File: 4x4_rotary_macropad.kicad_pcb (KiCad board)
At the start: 4 copper layers, 77.1 x 116.4 mm, 81 parts, among them J1 Conn_01x04_Pin, J2 Conn_01x04_Socket, SW1 SW_Push, SW10 SW_Push, SW11 SW_Push, SW12 SW_Push, SW13 SW_Push, SW14 SW_Push, SW15 SW_Push, SW16 SW_Push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

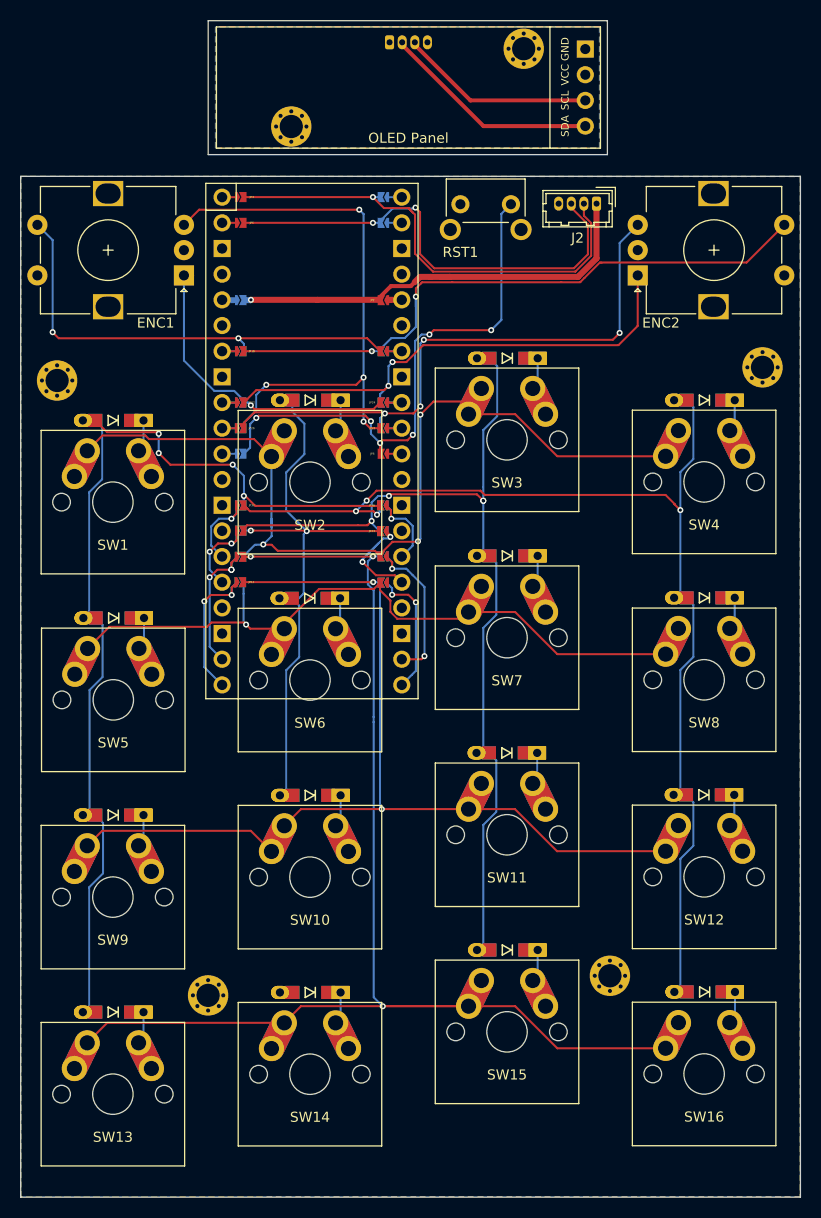
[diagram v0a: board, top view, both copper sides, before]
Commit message: Fixed JLCPCB constraints errors
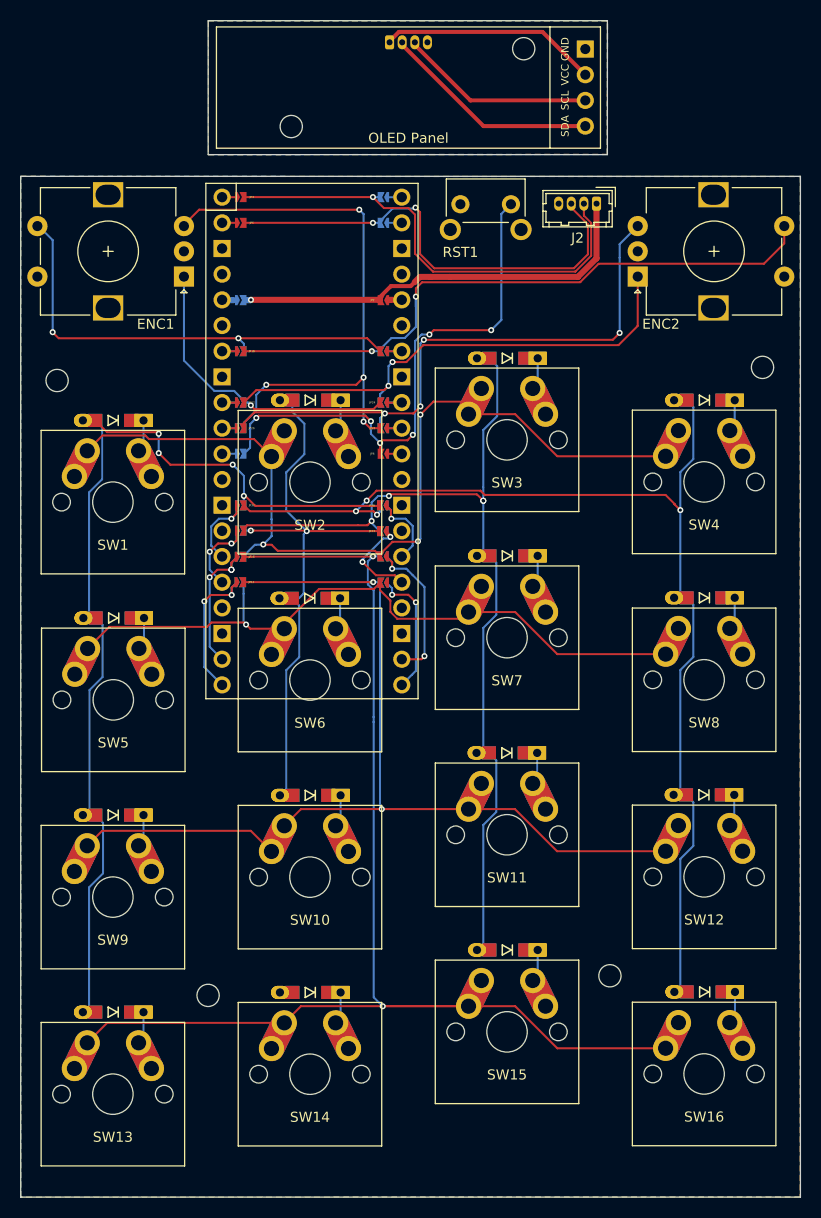
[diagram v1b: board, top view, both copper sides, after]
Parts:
- H1, H2, H3, H4, H5, H6: footprint kbd:M2_HOLE_v3 -> MountingHole:MountingHole_2.2mm_M2
- moved ENC1 0.12 mm to (44.4, 68.1)
- moved ENC2 0.12 mm to (89.2, 68.1)
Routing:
- net /B_VCC: track 0.00 -> 21.6 mm
- net C2_C1: track 11.7 -> 10.2 mm
- net R1__R2: track 16.4 -> 15.2 mm
- net ENC_1_A: track 31.3 -> 30.2 mm
- net R0: track 88.6 -> 87.5 mm
- net VCC: track 42.9 -> 42.0 mm
- net OLED_SDA: track 47.1 -> 46.5 mm
- net ENC_2_A: track 50.7 -> 50.1 mm
- net C3: track 110.6 -> 110.1 mm
- net ENC_2_SW: track 62.7 -> 63.3 mm
- net R3: vias 3 -> 2
- added copper zone on F.Cu, net /B_GND
- removed copper zone on F.Cu, net /B_VCC

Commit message: Added missing libraries
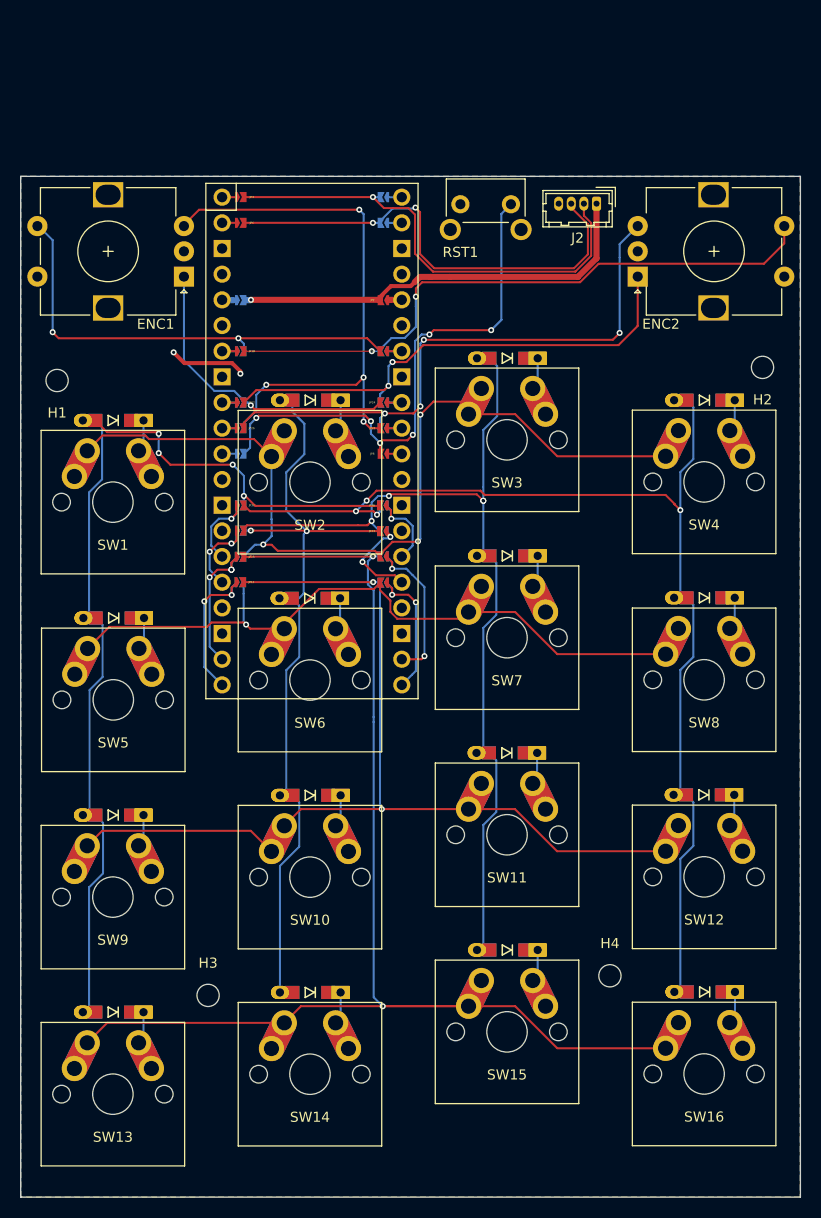
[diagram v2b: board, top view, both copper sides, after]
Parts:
- removed H5, H6: MountingHole, MountingHole:MountingHole_2.2mm_M2
- removed J1: Conn_01x04_Pin, Connector_Hirose:Hirose_DF13-04P-1.25DS_1x04_P1.25mm_Horizontal
- removed OLED1: OLED, KiCad-SSD1306-0.91-OLED-4pin-128x32:SSD1306-0.91-OLED-4pin-128x32
- U1: footprint MCU_RaspberryPi_and_Boards:RPi_Pico_SMD_TH -> cherry_with_keycap:RPi_Pico_SMD_TH
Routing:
- net /B_SDA: track 21.7 -> 0.00 mm
- net /B_VCC: track 21.6 -> 0.00 mm
- net C1: track 56.7 -> 77.3 mm
- net /B_SCK: track 19.4 -> 0.00 mm
- net GND: track 0.00 -> 7.61 mm, vias 0 -> 2
- net R2__R1: track 12.8 -> 14.3 mm
- removed copper zone on B.Cu, net /B_GND
- removed copper zone on F.Cu, net /B_GND
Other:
- board size 77.1 x 116.4 mm -> 77.1 x 101 mm

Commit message: Updated PCB properties
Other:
- copper layers 4 -> 2
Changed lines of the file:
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@@
   (layers
     (0 "F.Cu" signal "Front")
-    (1 "In1.Cu" signal)
-    (2 "In2.Cu" signal)
     (31 "B.Cu" signal "Back")
     (34 "B.Paste" user)
@@
       (layer "F.Mask" (type "Top Solder Mask") (thickness 0.01))
       (layer "F.Cu" (type "copper") (thickness 0.035))
-      (layer "dielectric 1" (type "core") (thickness 1.51) (material "FR4") (epsilon_r 4.5) (loss_tangent 0.02))
-      (layer "In1.Cu" (type "copper") (thickness 0.035))
-      (layer "dielectric 2" (type "prepreg") (thickness 1.51) (material "FR4") (epsilon_r 4.5) (loss_tangent 0.02))
-      (layer "In2.Cu" (type "copper") (thickness 0.035))
-      (layer "dielectric 3" (type "core") (thickness 1.51) (material "FR4") (epsilon_r 4.5) (loss_tangent 0.02))
+      (layer "dielectric 1" (type "core") (thickness 4.6) (material "FR4") (epsilon_r 4.5) (loss_tangent 0.02))
       (layer "B.Cu" (type "copper") (thickness 0.035))
       (layer "B.Mask" (type "Bottom Solder Mask") (thickness 0.01))
@@
     (solder_mask_min_width 0.12)
     (pcbplotparams
-      (layerselection 0x002f0fc_ffffffff)
+      (layerselection 0x00010fc_ffffffff)
       (plot_on_all_layers_selection 0x0000000_00000000)
       (disableapertmacros false)
-      (usegerberextensions false)
+      (usegerberextensions true)
       (usegerberattributes true)
-      (usegerberadvancedattributes true)
-      (creategerberjobfile true)
+      (usegerberadvancedattributes false)
+      (creategerberjobfile false)
       (dashed_line_dash_ratio 12.000000)
       (dashed_line_gap_ratio 3.000000)
@@
       (psa4output false)
       (plotreference true)
-      (plotvalue true)
+      (plotvalue false)
       (plotinvisibletext false)
       (sketchpadsonfab false)
-      (subtractmaskfromsilk false)
+      (subtractmaskfromsilk true)
       (outputformat 1)
       (mirror false)
@@
   (segment (start 46.993961 99.625) (end 49.075 99.625) (width 0.2) (layer "F.Cu") (net 48))
   (segment (start 49.075 99.625) (end 49.075 98.885) (width 0.2) (layer "F.Cu") (net 48))
-  (segment (start 49.61 98.35) (end 49.61 98.615) (width 0.2) (layer "F.Cu") (net 48))
   (segment (start 49.075 98.885) (end 49.61 98.35) (width 0.2) (layer "F.Cu") (net 48))
   (via (at 46.368961 100.25) (size 0.6) (drill 0.3) (layers "F.Cu" "B.Cu") (net 48))
